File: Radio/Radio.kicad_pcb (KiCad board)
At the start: 2 copper layers, 17 parts, among them SW1 Bourns PEC11R, SW2 Bourns PEC11R, SW3 SW_Push, SW4 SW_Push, U1 LM386, U2 RDA5807M_Module

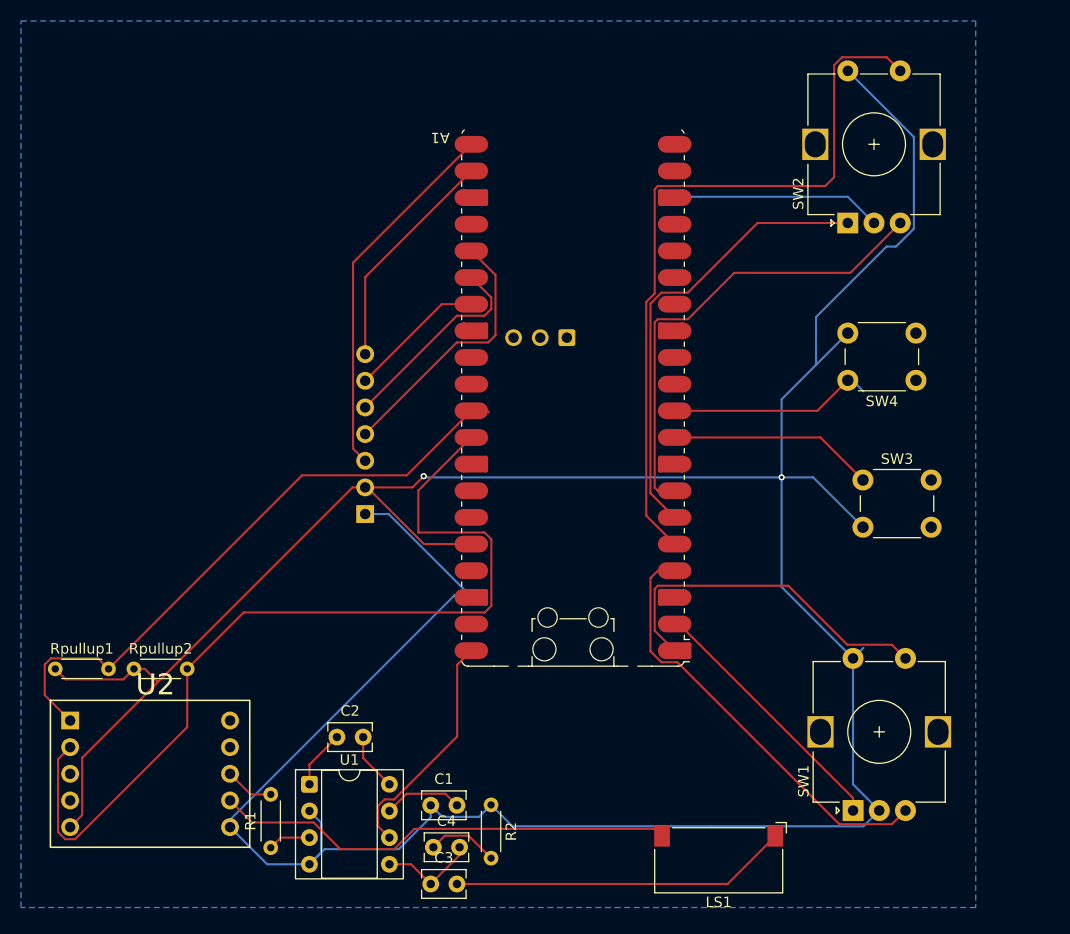
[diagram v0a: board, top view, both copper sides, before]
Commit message: Made PCB and moved a few gpio pins for buttons
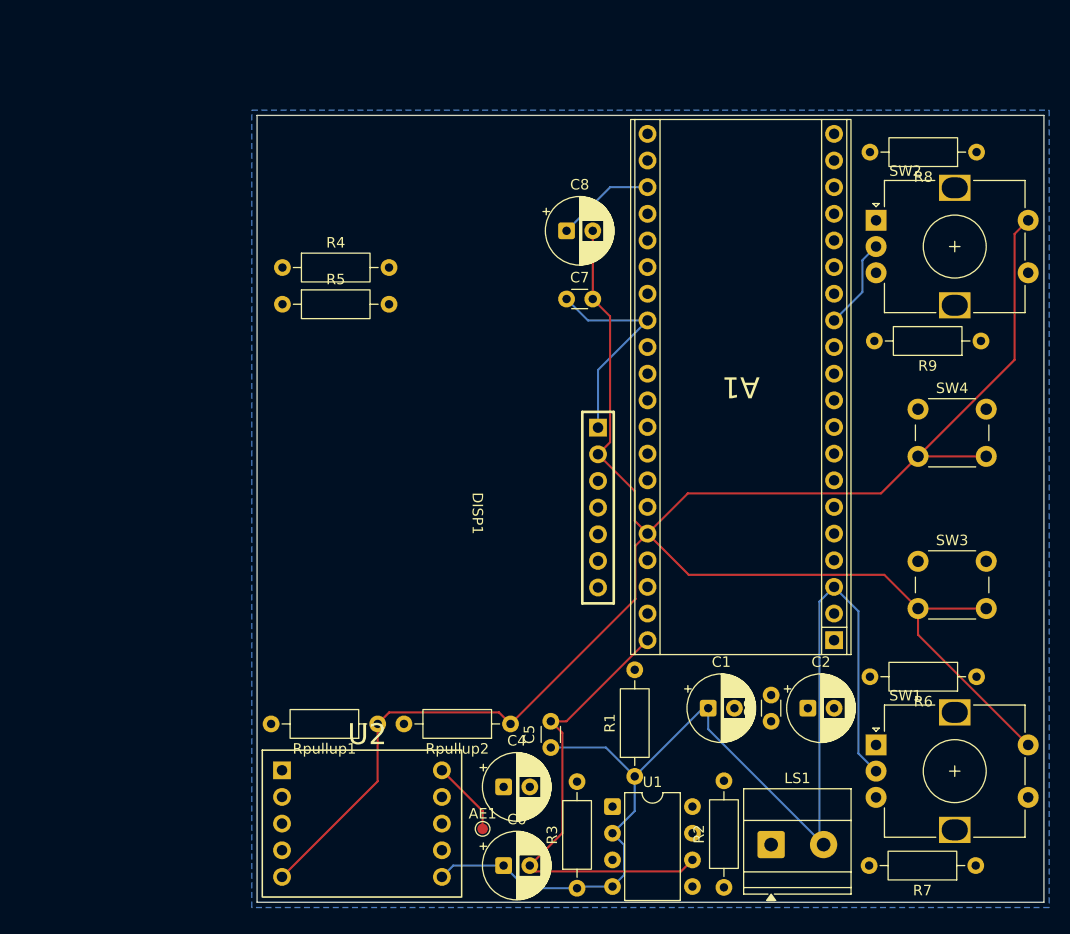
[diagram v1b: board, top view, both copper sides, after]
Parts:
- added AE1: Antenna, TestPoint:TestPoint_Pad_D1.0mm, F.Cu at (141.5, 123.0)
- added C5: 0.1uF, Capacitor_THT:C_Disc_D3.0mm_W1.6mm_P2.50mm, F.Cu at (148.0, 115.2)
- added C6: 470uF, Capacitor_THT:CP_Radial_D6.3mm_P2.50mm, F.Cu at (143.5, 126.5)
- added C7: 0.1uF, Capacitor_THT:C_Disc_D3.0mm_W1.6mm_P2.50mm, F.Cu at (149.5, 72.5)
- added C8: 470uF, Capacitor_THT:CP_Radial_D6.3mm_P2.50mm, F.Cu at (149.5, 66.0)
- added R3: 10K, Resistor_THT:R_Axial_DIN0207_L6.3mm_D2.5mm_P10.16mm_Horizontal, F.Cu at (150.5, 128.7)
- added R4: 10K, Resistor_THT:R_Axial_DIN0207_L6.3mm_D2.5mm_P10.16mm_Horizontal, F.Cu at (122.4, 69.5)
- added R5: 10K, Resistor_THT:R_Axial_DIN0207_L6.3mm_D2.5mm_P10.16mm_Horizontal, F.Cu at (122.4, 73.0)
- added R6: 10K, Resistor_THT:R_Axial_DIN0207_L6.3mm_D2.5mm_P10.16mm_Horizontal, F.Cu at (188.6, 108.5)
- added R7: 10K, Resistor_THT:R_Axial_DIN0207_L6.3mm_D2.5mm_P10.16mm_Horizontal, F.Cu at (188.5, 126.5)
- added R8: 10K, Resistor_THT:R_Axial_DIN0207_L6.3mm_D2.5mm_P10.16mm_Horizontal, F.Cu at (188.6, 58.5)
- added R9: 10K, Resistor_THT:R_Axial_DIN0207_L6.3mm_D2.5mm_P10.16mm_Horizontal, F.Cu at (189.0, 76.5)
- A1: footprint Module:RaspberryPi_Pico_W_SMD_HandSolder -> ECE:RPi_Pico_TH
- C1: value C_US -> 10uF; footprint Capacitor_THT:C_Rect_L4.0mm_W2.5mm_P2.50mm -> Capacitor_THT:CP_Radial_D6.3mm_P2.50mm
- C2: value 10uF -> 470uF; footprint Capacitor_THT:C_Rect_L4.0mm_W2.5mm_P2.50mm -> Capacitor_THT:CP_Radial_D6.3mm_P2.50mm
- C3: value 470uF -> 0.05uF; footprint Capacitor_THT:C_Rect_L4.0mm_W2.5mm_P2.50mm -> Capacitor_THT:C_Disc_D3.0mm_W1.6mm_P2.50mm
- C4: value 0.05uF -> 10uF; footprint Capacitor_THT:C_Rect_L4.0mm_W2.5mm_P2.50mm -> Capacitor_THT:CP_Radial_D6.3mm_P2.50mm
- DISP1: moved to F.Cu
- LS1: footprint Buzzer_Beeper:Speaker_CUI_CMR-1206S-67 -> TerminalBlock_Phoenix:TerminalBlock_Phoenix_MKDS-1,5-2_1x02_P5.00mm_Horizontal
- R1: value 10K -> 10; footprint Resistor_THT:R_Axial_DIN0204_L3.6mm_D1.6mm_P5.08mm_Horizontal -> Resistor_THT:R_Axial_DIN0207_L6.3mm_D2.5mm_P10.16mm_Horizontal
- R2: value 10 -> 1.2K; footprint Resistor_THT:R_Axial_DIN0204_L3.6mm_D1.6mm_P5.08mm_Horizontal -> Resistor_THT:R_Axial_DIN0207_L6.3mm_D2.5mm_P10.16mm_Horizontal
- Rpullup1, Rpullup2: footprint Resistor_THT:R_Axial_DIN0204_L3.6mm_D1.6mm_P5.08mm_Horizontal -> Resistor_THT:R_Axial_DIN0207_L6.3mm_D2.5mm_P10.16mm_Horizontal
- SW1, SW2: value Bourns PEC11R -> Rotary Encoder
- U1: footprint Package_DIP:DIP-8_W7.62mm_Socket -> Package_DIP:DIP-8_W7.62mm
- moved C2 45.0 mm to (172.5, 111.5)
- moved Rpullup2 36.3 mm to (144.2, 113.0), turned to 180 degrees
- moved DISP1 36.1 mm to (120.5, 74.6), turned to -90 degrees
- moved C3 36.0 mm to (169.0, 112.8), turned to 90 degrees
- moved R1 35.4 mm to (156.0, 118.0)
- moved Rpullup1 31.2 mm to (131.5, 113.0), turned to 180 degrees
- moved U1 29.0 mm to (153.9, 120.9)
- moved C1 28.0 mm to (163.0, 111.5)
- moved R2 23.5 mm to (164.5, 128.6), turned to 90 degrees
- moved U2 20.7 mm to (130.0, 122.5)
- moved A1 16.0 mm to (166.1, 80.9)
- moved SW3 9.36 mm to (183.0, 97.5)
- moved C4 8.83 mm to (143.5, 119.0)
- moved SW1 6.63 mm to (179.0, 115.0), turned to 0 degrees
- moved LS1 5.22 mm to (169.0, 124.5), turned to 0 degrees
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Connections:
- A1 pad 17: unconnected-(A1-GPIO13-Pad17) -> Net-(A1-GPIO13)
- A1 pad 19: unconnected-(A1-GPIO14-Pad19) -> Net-(A1-GPIO14)
- A1 pad 20: unconnected-(A1-GPIO15-Pad20) -> Net-(A1-GPIO15)
- A1 pad 6: Net-(A1-GPIO4) -> unconnected-(A1-GPIO4-Pad6)
- A1 pad 7: Net-(A1-GPIO5) -> unconnected-(A1-GPIO5-Pad7)
- A1 pad 9: Net-(A1-GPIO6) -> unconnected-(A1-GPIO6-Pad9)
- C3 pad 2: Net-(C3-Pad2) -> Net-(C2-Pad1)
- C4 pad 2: Net-(C3-Pad1) -> Net-(U1-+)
- LS1 pad 1: Net-(C3-Pad2) -> Net-(C2-Pad2)
- LS1 pad 2: Net-(U2-ROUT) -> Net-(DISP1-VSS/GND)
- R1 pad 1: Net-(U1-+) -> Net-(DISP1-VSS/GND)
- R1 pad 2: Net-(U1-+) -> Net-(C3-Pad1)
- R2 pad 1: Net-(DISP1-VSS/GND) -> Net-(R2-Pad1)
- R2 pad 2: Net-(C4-Pad1) -> Net-(R2-Pad2)
- SW1 pad A: Net-(A1-GPIO1) -> Net-(R6-Pad1)
- SW1 pad B: Net-(A1-GPIO2) -> Net-(R7-Pad1)
- SW2 pad A: Net-(A1-GPIO4) -> Net-(R8-Pad1)
- SW2 pad B: Net-(A1-GPIO5) -> Net-(R9-Pad1)
- SW2 pad S2: Net-(A1-GPIO3) -> Net-(A1-GPIO13)
- SW3 pad 1: Net-(A1-GPIO6) -> Net-(A1-GPIO3)
- U1 pad 1: Net-(C2-Pad1) -> Net-(R2-Pad1)
- U1 pad 5: Net-(C3-Pad1) -> Net-(C2-Pad1)
- U1 pad 8: Net-(C2-Pad2) -> Net-(R2-Pad2)
- U2 pad 10: unconnected-(U2-FMIN-Pad10) -> Net-(AE1-A)
- U2 pad 8: Net-(U1-+) -> Net-(U2-LOUT)
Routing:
- net Net-(C4-Pad1): track 6.84 -> 75.2 mm
- net Net-(U2-LOUT): track 0.00 -> 56.0 mm
- net Net-(A1-GPIO3): track 70.7 -> 15.6 mm
- net Net-(A1-GPIO5): track 45.1 -> 0.00 mm
- net Net-(A1-GPIO4): track 43.3 -> 0.00 mm
- net Net-(A1-GPIO27_ADC1): track 87.3 -> 53.0 mm
- net Net-(C2-Pad1): track 5.59 -> 38.0 mm
- net Net-(C3-Pad2): track 32.2 -> 0.00 mm
- net Net-(A1-GPIO13): track 0.00 -> 31.2 mm
- net Net-(A1-GPIO17): track 21.7 -> 52.9 mm
- net Net-(A1-GPIO15): track 0.00 -> 22.7 mm
- net Net-(A1-VBUS): track 22.5 -> 44.1 mm
- net Net-(A1-GPIO6): track 19.6 -> 0.00 mm
- net Net-(A1-GPIO20): track 19.7 -> 37.7 mm
- net Net-(A1-GPIO1): track 25.1 -> 7.44 mm
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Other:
- board outline added: 75 x 75 mm
- copper layers 2 -> 4
